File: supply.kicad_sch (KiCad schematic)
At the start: 71 parts, among them Q6 DMG1012T-7, U4 TPS2117DRLR, U5 TPS2117DRLR, U6 PAC1934T_WLCSP, U7 MP5424GRM, U8 MP8869S

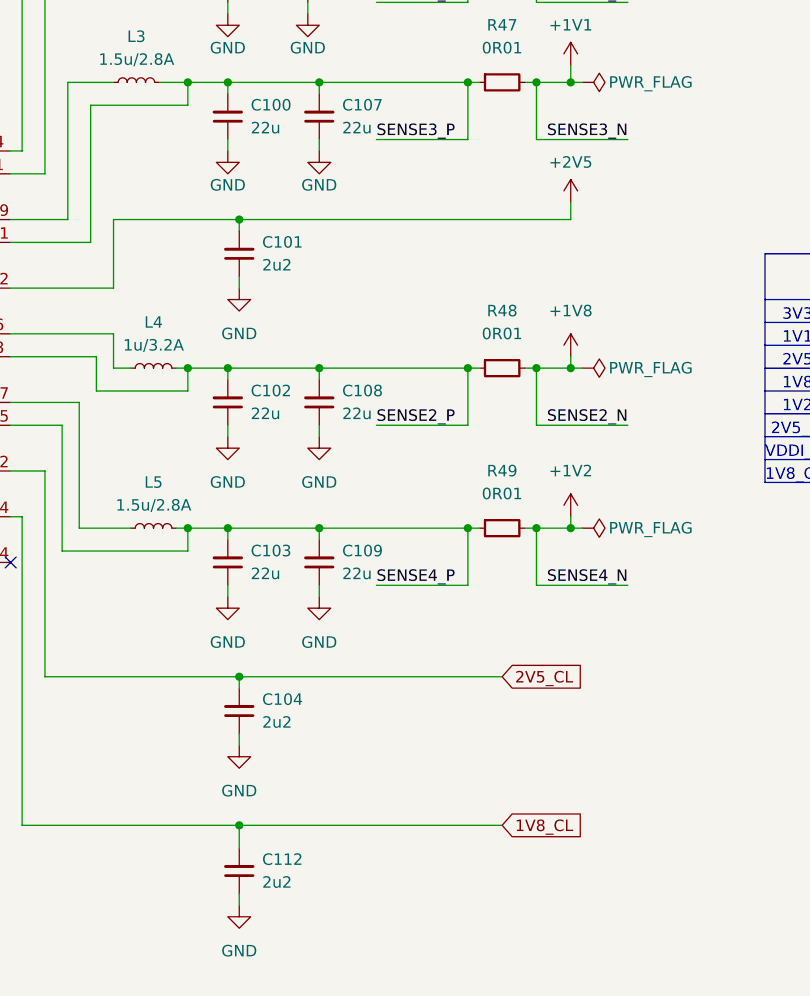
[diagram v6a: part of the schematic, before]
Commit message: [#59453] Add 0R on +2V5, 2V5_CL and 1V8_CL rails
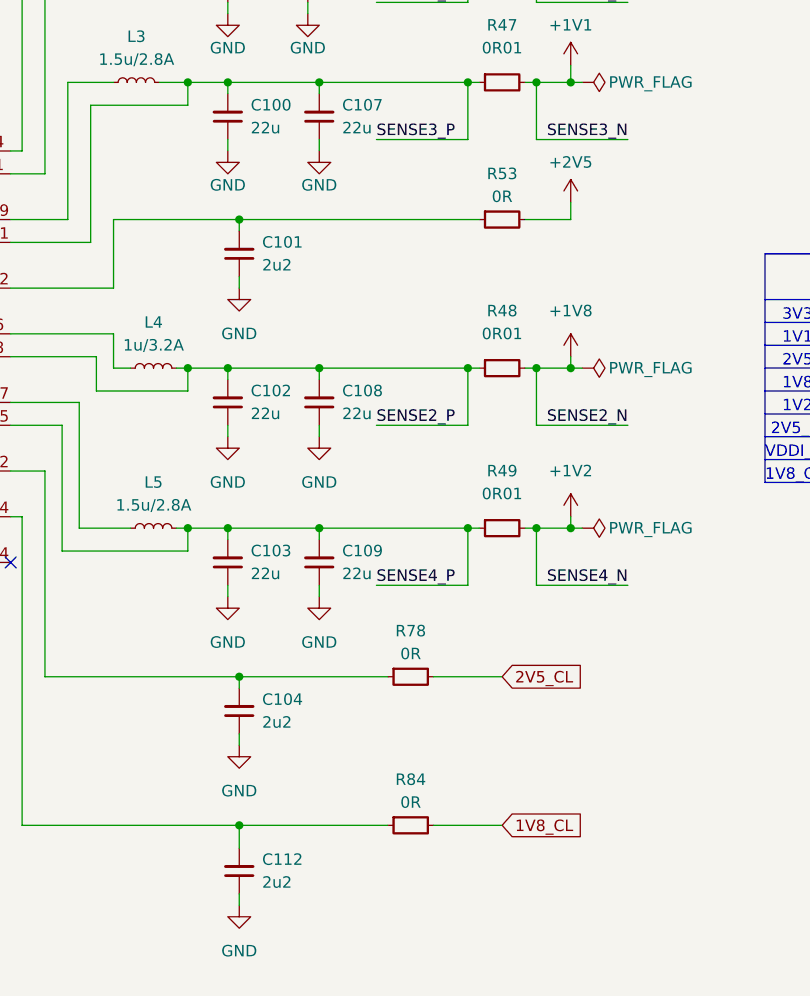
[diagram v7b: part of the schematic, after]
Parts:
- added R53: R_0R_22.4A_0603, antmicro-footprints:R_0603_1608Metric, symbol antmicroResistors0603:R_0R_22.4A_0603
- added R78, R84: R_0R_0402, antmicro-footprints:R_0402_1005Metric, symbol antmicroResistors0402:R_0R_0402
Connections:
- net +2V5: now also R53.2; no longer C101.2, U7.22 (OUT2)
- net 1V8_CL: now also R84.2; no longer C112.2, U7.14 (OUT5)
- net 2V5_CL: now also R78.2; no longer C104.2, U7.12 (OUT4)
- new net: C112.2, R84.1, U7.14 (OUT5)
- new net: C101.2, R53.1, U7.22 (OUT2)
- new net: C104.2, R78.1, U7.12 (OUT4)
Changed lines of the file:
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@@
     (stroke (width 0) (type default))
   )
-  (wire (pts (xy 262.89 143.51) (xy 292.1 143.51))
+  (wire (pts (xy 262.89 143.51) (xy 279.4 143.51))
     (stroke (width 0) (type default))
   )
@@
     (stroke (width 0) (type default))
   )
-  (wire (pts (xy 262.89 127) (xy 292.1 127))
+  (wire (pts (xy 262.89 127) (xy 279.4 127))
     (stroke (width 0) (type default))
   )
@@
     (stroke (width 0) (type default))
   )
+  (wire (pts (xy 294.64 76.2) (xy 299.72 76.2))
+    (stroke (width 0) (type default))
+  )
   (wire (pts (xy 261.62 92.71) (xy 261.62 93.98))
     (stroke (width 0) (type default))
@@
     (stroke (width 0) (type default))
   )
-  (wire (pts (xy 262.89 76.2) (xy 299.72 76.2))
+  (wire (pts (xy 262.89 76.2) (xy 289.56 76.2))
     (stroke (width 0) (type default))
   )
@@
     (stroke (width 0) (type default))
   )
+  (wire (pts (xy 284.48 127) (xy 292.1 127))
+    (stroke (width 0) (type default))
+  )
   (bus (pts (xy 192.405 121.285) (xy 193.675 121.285))
     (stroke (width 0) (type default))
@@
     (stroke (width 0) (type default))
   )
+  (wire (pts (xy 284.48 143.51) (xy 292.1 143.51))
+    (stroke (width 0) (type default))
+  )
   (wire (pts (xy 245.11 96.52) (xy 245.11 110.49))
     (stroke (width 0) (type default))
@@
     )
   )
+  (symbol (lib_id "antmicroResistors0402:R_0R_0402") (at 279.4 143.51 0) (unit 1)
+    (in_bom yes) (on_board yes) (dnp no)
+    (property "Reference" "R84" (at 281.94 138.43 0)
+      (effects (font (size 1.27 1.27) (thickness 0.15)))
+    )
+    (property "Value" "R_0R_0402" (at 299.72 156.21 0)
+      (effects (font (size 1.27 1.27) (thickness 0.15)) (justify left bottom) hide)
+    )
+    (property "Footprint" "antmicro-footprints:R_0402_1005Metric" (at 299.72 158.75 0)
+      (effects (font (size 1.27 1.27) (thickness 0.15)) (justify left bottom) hide)
+    )
+    (property "Datasheet" "https://industrial.panasonic.com/cdbs/www-data/pdf/RDA0000/AOA0000C301.pdf" (at 299.72 161.29 0)
+      (effects (font (size 1.27 1.27) (thickness 0.15)) (justify left bottom) hide)
+    )
+    (property "MPN" "ERJ2GE0R00X" (at 299.72 163.83 0)
+      (effects (font (size 1.27 1.27) (thickness 0.15)) (justify left bottom) hide)
+    )
+    (property "Manufacturer" "Panasonic" (at 299.72 166.37 0)
+      (effects (font (size 1.27 1.27) (thickness 0.15)) (justify left bottom) hide)
+    )
+    (property "License" "Apache-2.0" (at 299.72 168.91 0)
+      (effects (font (size 1.27 1.27) (thickness 0.15)) (justify left bottom) hide)
+    )
+    (property "Author" "Antmicro" (at 299.72 171.45 0)
+      (effects (font (size 1.27 1.27) (thickness 0.15)) (justify left bottom) hide)
+    )
+    (property "Val" "0R" (at 281.94 140.97 0)
+      (effects (font (size 1.27 1.27) (thickness 0.15)))
+    )
+    (property "Tolerance" "~" (at 299.72 153.67 0)
+      (effects (font (size 1.27 1.27)) (justify left bottom) hide)
+    )
+    (property "Current" "1A" (at 299.72 173.99 0)
+      (effects (font (size 1.27 1.27) (thickness 0.15)) (justify left bottom) hide)
+    )
+    (pin "1")
+    (pin "2")
+    (instances
+      (project "polarfire-som"
+        (path "/db4a0d3e-2eb3-499e-977d-6eb378cfd3ed/aa0aa716-c477-450b-ad01-6403345c3aae"
+          (reference "R84") (unit 1)
+        )
+      )
+    )
+  )
   (symbol (lib_id "antmicroResistors0402:R_10k_0402") (at 354.33 140.97 90) (unit 1)
     (in_bom yes) (on_board yes) (dnp no) (fields_autoplaced)
@@
     )
   )
+  (symbol (lib_id "antmicroResistors0603:R_0R_22.4A_0603") (at 289.56 76.2 0) (unit 1)
+    (in_bom yes) (on_board yes) (dnp no)
+    (property "Reference" "R53" (at 292.1 71.12 0)
+      (effects (font (size 1.27 1.27) (thickness 0.15)))
+    )
+    (property "Value" "R_0R_22.4A_0603" (at 292.1 67.31 0)
+      (effects (font (size 1.27 1.27) (thickness 0.15)) hide)
+    )
+    (property "Footprint" "antmicro-footprints:R_0603_1608Metric" (at 304.8 86.36 0)
+      (effects (font (size 1.27 1.27) (thickness 0.15)) (justify left bottom) hide)
+    )
+    (property "Datasheet" "https://fscdn.rohm.com/en/products/databook/datasheet/passive/resistor/chip_resistor/pmr-jpw-e.pdf" (at 304.8 88.9 0)
+      (effects (font (size 1.27 1.27) (thickness 0.15)) (justify left bottom) hide)
+    )
+    (property "MPN" "PMR03EZPJ000" (at 304.8 91.44 0)
+      (effects (font (size 1.27 1.27) (thickness 0.15)) (justify left bottom) hide)
+    )
+    (property "Manufacturer" "ROHM Semiconductor" (at 304.8 93.98 0)
+      (effects (font (size 1.27 1.27) (thickness 0.15)) (justify left bottom) hide)
+    )
+    (property "Val" "0R" (at 292.1 73.66 0)
+      (effects (font (size 1.27 1.27) (thickness 0.15)))
+    )
+    (property "Max. Curr." "22.4A" (at 297.18 78.74 0)
+      (effects (font (size 1.27 1.27) (thickness 0.15)) hide)
+    )
+    (property "Author" "Antmicro" (at 304.8 99.06 0)
+      (effects (font (size 1.27 1.27) (thickness 0.15)) (justify left bottom) hide)
+    )
+    (property "License" "Apache-2.0" (at 304.8 101.6 0)
+      (effects (font (size 1.27 1.27) (thickness 0.15)) (justify left bottom) hide)
+    )
+    (property "Tolerance" "template_tolerance" (at 309.88 86.36 0)
+      (effects (font (size 1.27 1.27)) (justify left bottom) hide)
+    )
+    (pin "1")
+    (pin "2")
+    (instances
+      (project "polarfire-som"
+        (path "/db4a0d3e-2eb3-499e-977d-6eb378cfd3ed/aa0aa716-c477-450b-ad01-6403345c3aae"
+          (reference "R53") (unit 1)
+        )
+      )
+    )
+  )
   (symbol (lib_id "antmicroCapacitors0402:C_22u_0402") (at 189.23 215.265 90) (unit 1)
     (in_bom yes) (on_board yes) (dnp no) (fields_autoplaced)
@@
         )
       )
+    )
+  )
+  (symbol (lib_id "antmicroResistors0402:R_0R_0402") (at 279.4 127 0) (unit 1)
+    (in_bom yes) (on_board yes) (dnp no)
+    (property "Reference" "R78" (at 281.94 121.92 0)
+      (effects (font (size 1.27 1.27) (thickness 0.15)))
+    )
+    (property "Value" "R_0R_0402" (at 299.72 139.7 0)
+      (effects (font (size 1.27 1.27) (thickness 0.15)) (justify left bottom) hide)
+    )
+    (property "Footprint" "antmicro-footprints:R_0402_1005Metric" (at 299.72 142.24 0)
+      (effects (font (size 1.27 1.27) (thickness 0.15)) (justify left bottom) hide)
+    )
+    (property "Datasheet" "https://industrial.panasonic.com/cdbs/www-data/pdf/RDA0000/AOA0000C301.pdf" (at 299.72 144.78 0)
+      (effects (font (size 1.27 1.27) (thickness 0.15)) (justify left bottom) hide)
+    )
+    (property "MPN" "ERJ2GE0R00X" (at 299.72 147.32 0)
+      (effects (font (size 1.27 1.27) (thickness 0.15)) (justify left bottom) hide)
+    )
+    (property "Manufacturer" "Panasonic" (at 299.72 149.86 0)
+      (effects (font (size 1.27 1.27) (thickness 0.15)) (justify left bottom) hide)
+    )
+    (property "License" "Apache-2.0" (at 299.72 152.4 0)
+      (effects (font (size 1.27 1.27) (thickness 0.15)) (justify left bottom) hide)
+    )
+    (property "Author" "Antmicro" (at 299.72 154.94 0)
+      (effects (font (size 1.27 1.27) (thickness 0.15)) (justify left bottom) hide)
+    )
+    (property "Val" "0R" (at 281.94 124.46 0)
+      (effects (font (size 1.27 1.27) (thickness 0.15)))
+    )
+    (property "Tolerance" "~" (at 299.72 137.16 0)
+      (effects (font (size 1.27 1.27)) (justify left bottom) hide)
+    )
+    (property "Current" "1A" (at 299.72 157.48 0)
+      (effects (font (size 1.27 1.27) (thickness 0.15)) (justify left bottom) hide)
+    )
+    (pin "1")
+    (pin "2")
+    (instances
+      (project "polarfire-som"
+        (path "/db4a0d3e-2eb3-499e-977d-6eb378cfd3ed/aa0aa716-c477-450b-ad01-6403345c3aae"
+          (reference "R78") (unit 1)
+        )
+      )

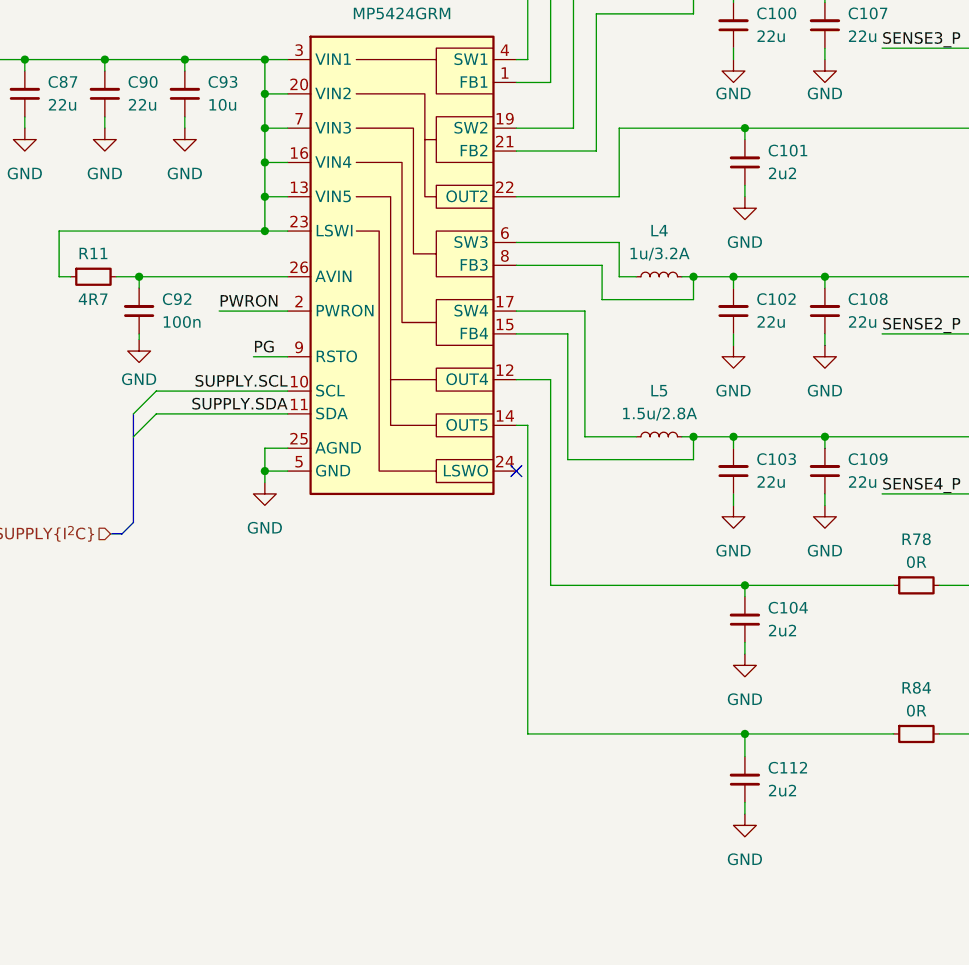
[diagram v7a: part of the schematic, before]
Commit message: [#59457] Optimize BOM
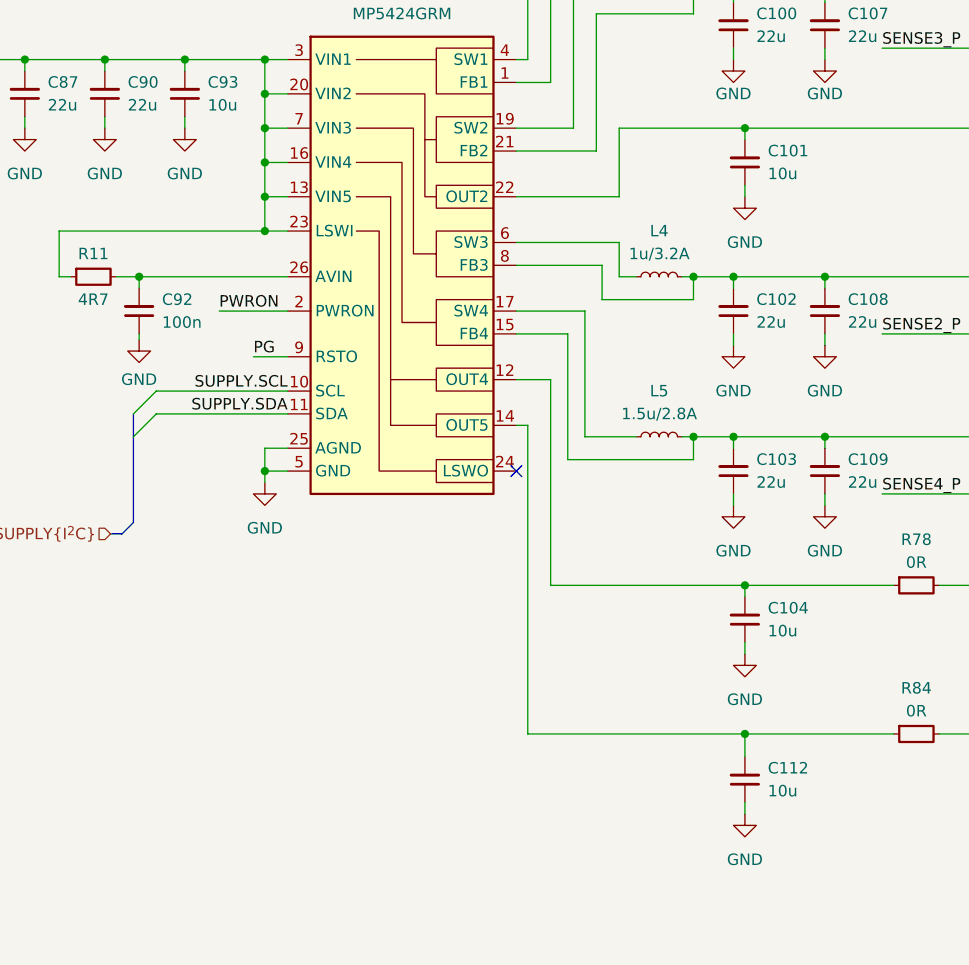
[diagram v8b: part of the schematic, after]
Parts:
- removed C101, C104, C112: C_2u2_0402, antmicro-footprints:C_0402_1005Metric, symbol antmicroCapacitors0402:C_2u2_0402
- removed C92: C_100n_25V_0402, antmicro-footprints:C_0402_1005Metric, symbol antmicroCapacitors0402:C_100n_25V_0402
- added C101, C104, C112: C_10u_10V_0402, antmicro-footprints:C_0402_1005Metric, symbol antmicroCapacitors0402:C_10u_10V_0402
- added C92: C_100n_0402, antmicro-footprints:C_0402_1005Metric, symbol antmicroCapacitors0402:C_100n_0402
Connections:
- net GND: now also C101.1, C104.1, C112.1, C92.1
- net at R84.1, U7.14 (OUT5): now also C112.2
- net at R53.1, U7.22 (OUT2): now also C101.2
- net at R78.1, U7.12 (OUT4): now also C104.2
- net at R11.2, U7.26 (AVIN): now also C92.2
